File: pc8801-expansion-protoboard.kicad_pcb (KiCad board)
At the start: 2 copper layers, 219 x 95 mm, 45 parts, among them J1 Solder Side, J2 Parts Side, J3 5V, J4 12V, J5 -12V, J6 GND_1, J7 GND_2, SW1 Reset ESP, U1 ExpansionEdge, U10 74LS165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

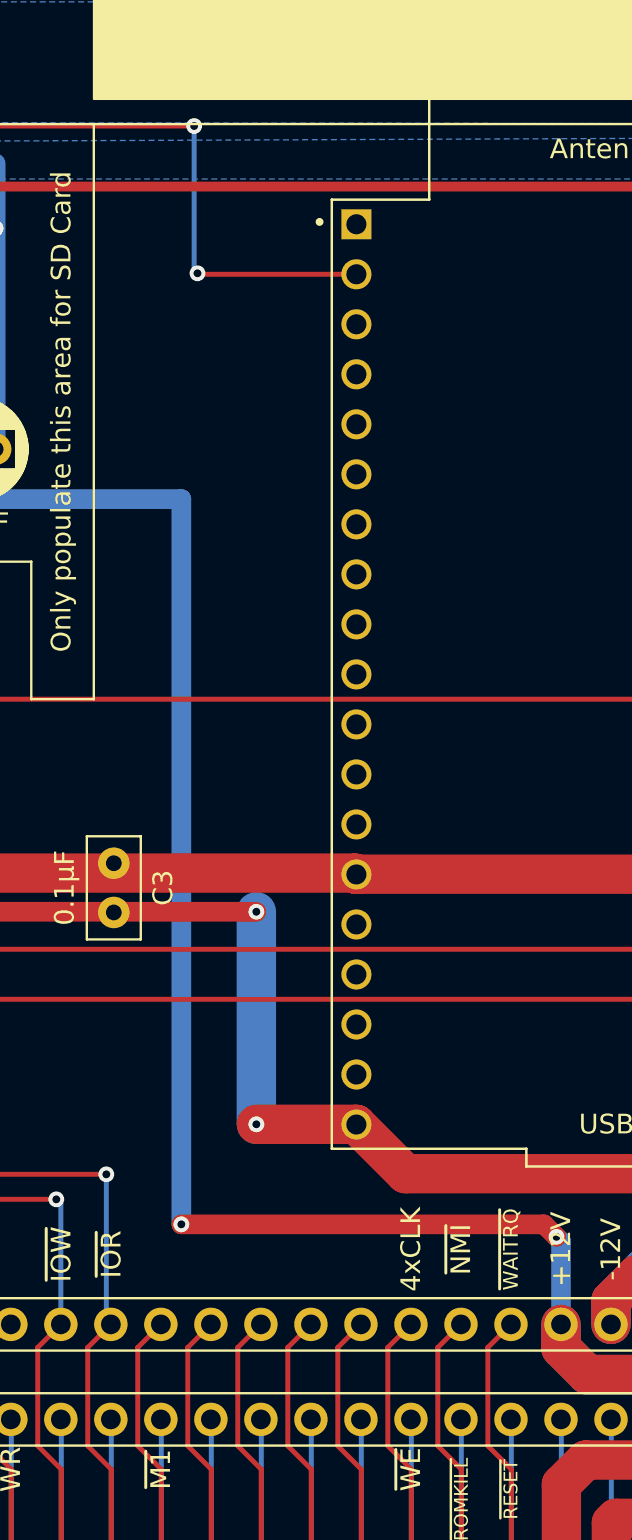
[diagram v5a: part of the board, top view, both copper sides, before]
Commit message: Wire ESP32 to system reset
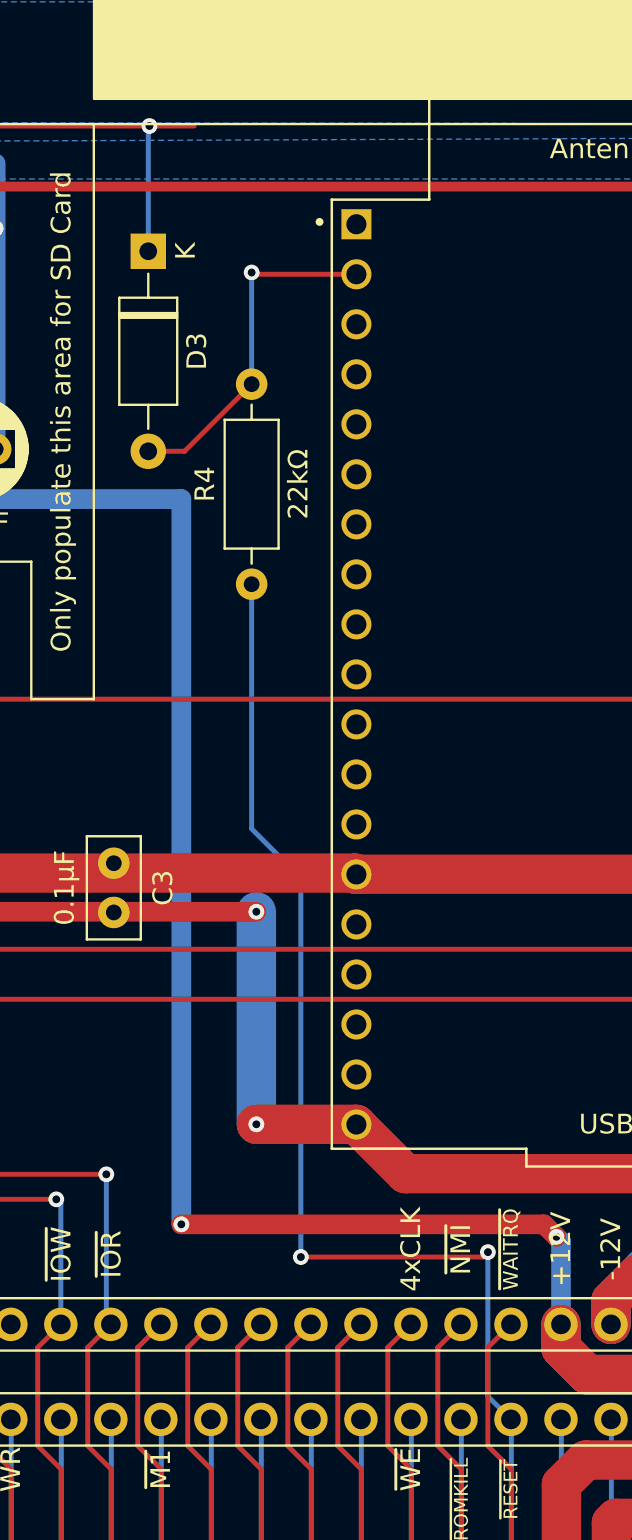
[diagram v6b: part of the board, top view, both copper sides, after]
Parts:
- added D3: D, Diode_THT:D_A-405_P10.16mm_Horizontal, F.Cu at (168.5, 67.4)
- added R4: 22kΩ, Resistor_THT:R_Axial_DIN0207_L6.3mm_D2.5mm_P10.16mm_Horizontal, F.Cu at (173.8, 84.3)
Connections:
- net Net-(J1-Pad32) renamed /~{RESET}
- SW1 pad 2: /~{ESP_RESET} -> Net-(SW1-Pad2)
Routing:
- net /~{RESET}: track 11.8 -> 65.6 mm, vias 0 -> 2
- net Net-(SW1-Pad2): track 0.00 -> 51.8 mm, vias 0 -> 3
- net /~{ESP_RESET}: track 61.1 -> 17.7 mm, vias 4 -> 1

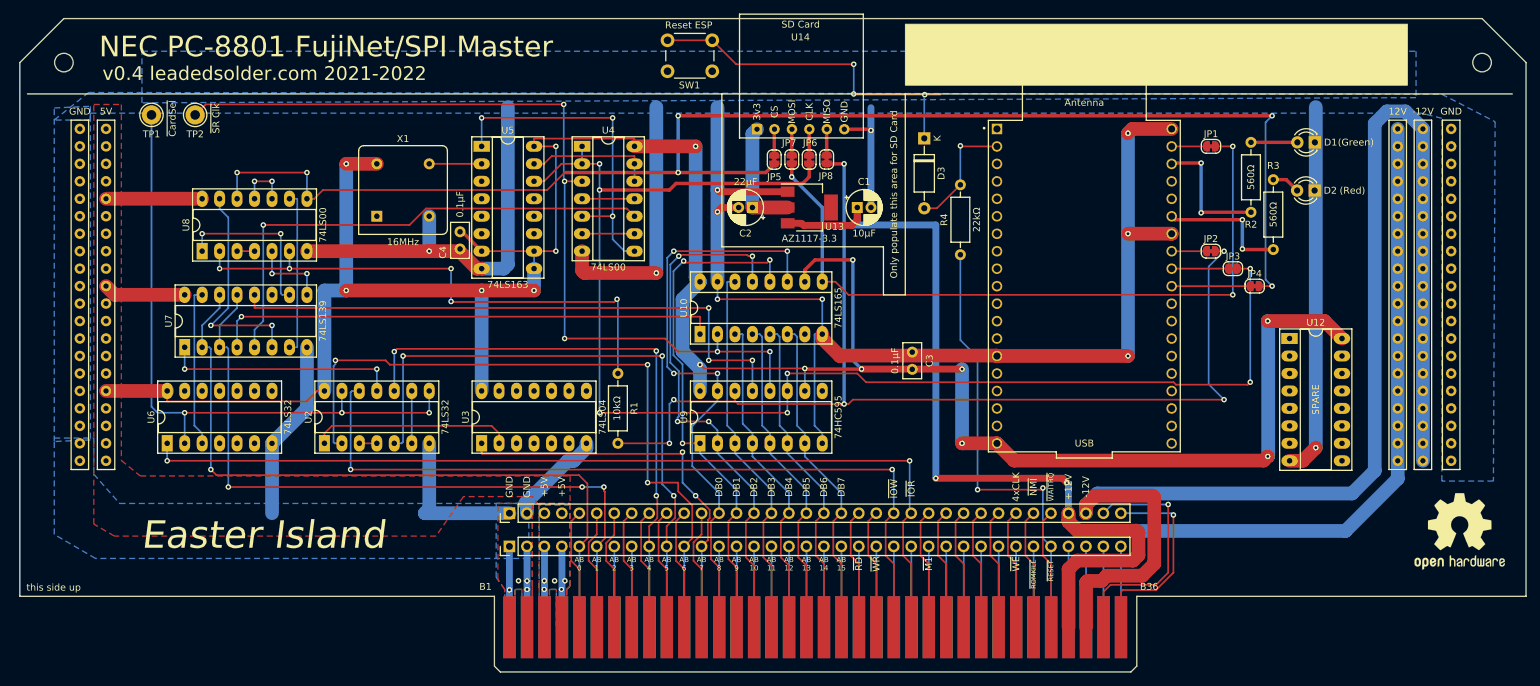
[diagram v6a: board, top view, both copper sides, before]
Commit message: As per Collapse, jumper-able clocks
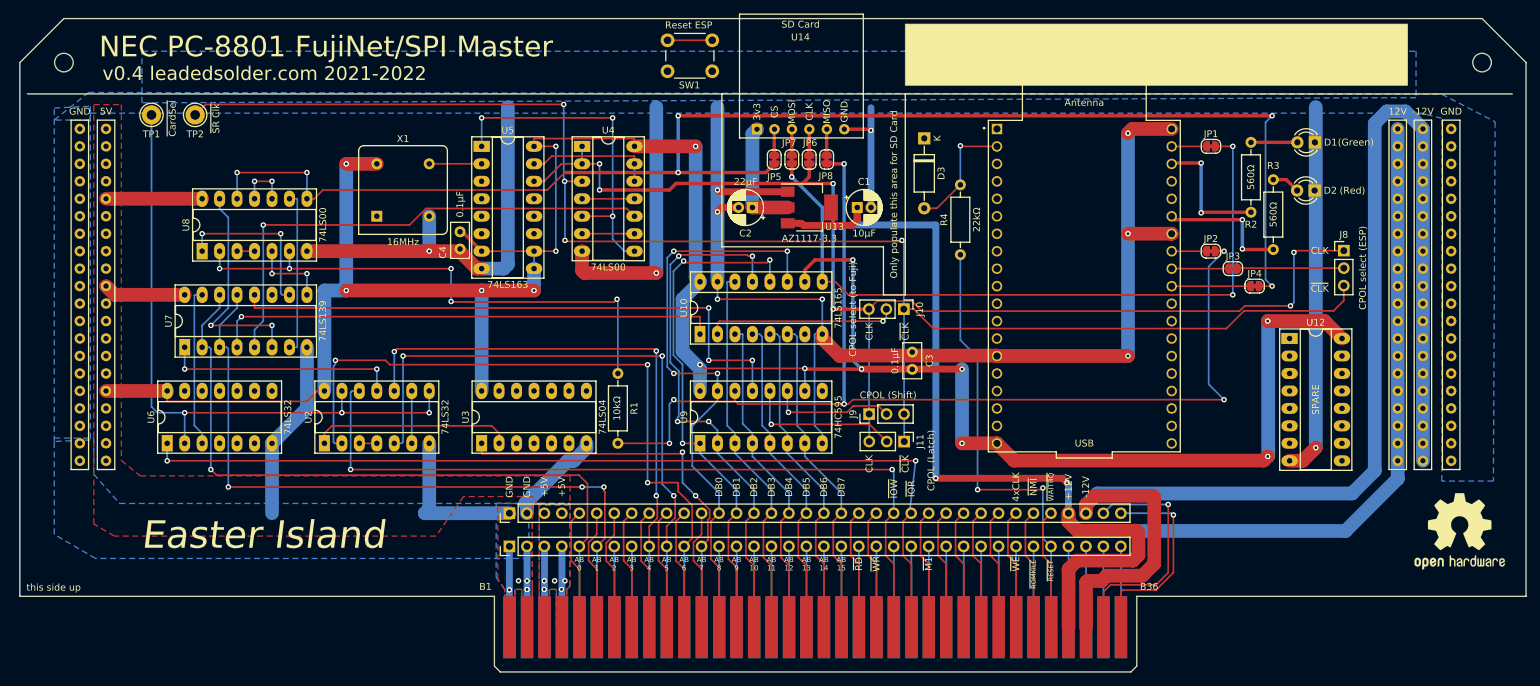
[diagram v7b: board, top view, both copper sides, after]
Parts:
- added J10: CPOL select (to Fuji), Connector_PinHeader_2.54mm:PinHeader_1x03_P2.54mm_Vertical, F.Cu at (165.5, 92.2)
- added J11: CPOL (Latch), Connector_PinHeader_2.54mm:PinHeader_1x03_P2.54mm_Vertical, F.Cu at (165.6, 111.5)
- added J8: CPOL select (ESP), Connector_PinHeader_2.54mm:PinHeader_1x03_P2.54mm_Vertical, F.Cu at (229.5, 83.8)
- added J9: CPOL (Shift), Connector_PinHeader_2.54mm:PinHeader_1x03_P2.54mm_Vertical, F.Cu at (160.5, 107.5)
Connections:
- JP3 pad 2: /SPI_CLK -> /OUT_CLOCK
- U10 pad 2: /~{SPI_CLK} -> /IN_CLOCK
- U9 pad 11: /SPI_CLK -> /SRCLK
- U9 pad 12: /~{SPI_CLK} -> /RCLK
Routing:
- net /~{SPI_CLK}: track 129.7 -> 224.1 mm, vias 5 -> 4
- net Net-(D3-Pad1): track 51.8 -> 6.50 mm, vias 3 -> 0
- net /IN_CLOCK: track 0.00 -> 27.7 mm, vias 0 -> 1
- net /SPI_CLK: track 202.0 -> 175.3 mm, vias 7 -> 6
- net /RCLK: track 0.00 -> 22.8 mm, vias 0 -> 1
- net /SRCLK: track 0.00 -> 18.3 mm, vias 0 -> 1
- net /OUT_CLOCK: track 0.00 -> 15.5 mm
- net /~{IOR}: track 135.8 -> 136.7 mm

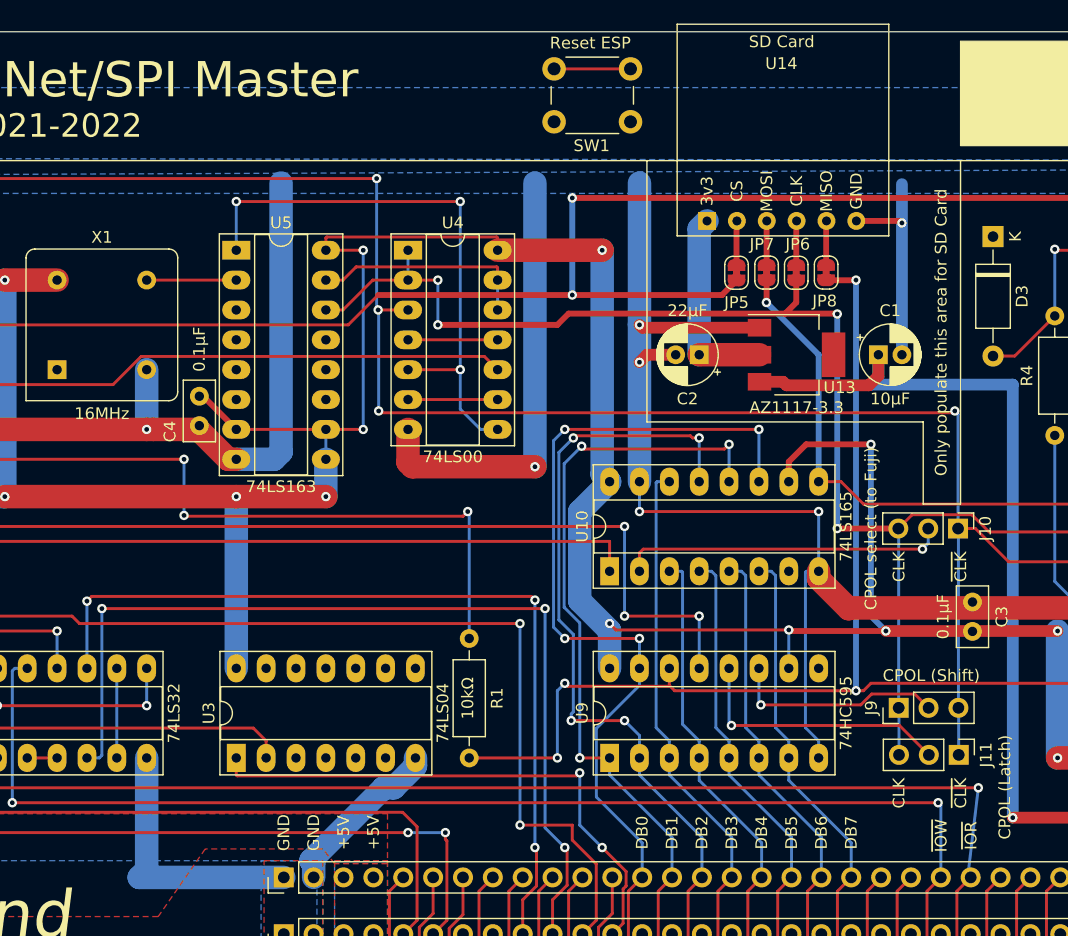
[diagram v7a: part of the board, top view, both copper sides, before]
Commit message: Jumper to disable PU/PD
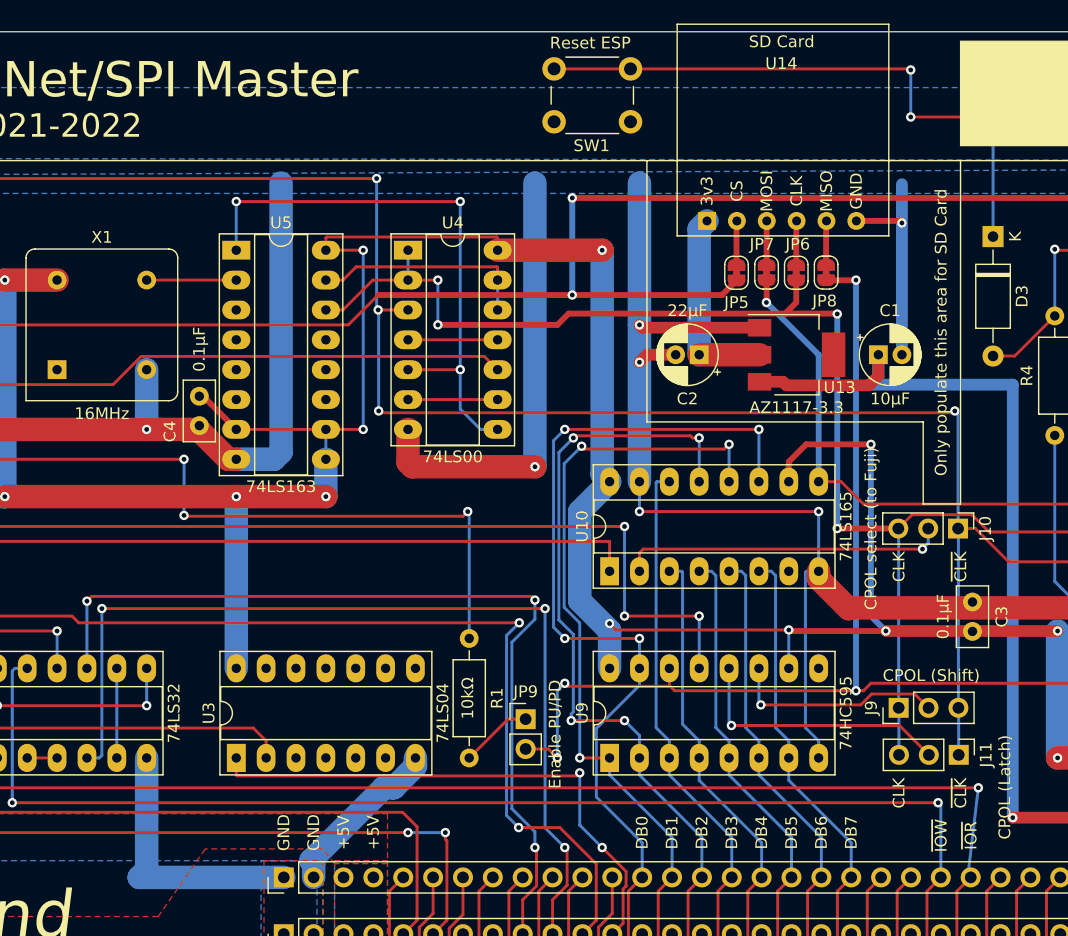
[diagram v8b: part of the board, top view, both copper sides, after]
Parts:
- added JP9: Enable PU/PD, Connector_PinHeader_2.54mm:PinHeader_1x02_P2.54mm_Vertical, F.Cu at (128.8, 108.5)
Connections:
- R1 pad 2: /FUJI_OUT -> Net-(R1-Pad2)
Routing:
- net Net-(D3-Pad1): track 6.50 -> 51.5 mm, vias 0 -> 3
- net Net-(R1-Pad2): track 0.00 -> 6.16 mm
- net /FUJI_OUT: track 158.3 -> 153.9 mm
- net /A4: track 84.8 -> 86.5 mm
